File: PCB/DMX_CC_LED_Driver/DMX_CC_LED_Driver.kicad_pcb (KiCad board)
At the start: 2 copper layers, 100 x 45 mm, 46 parts, among them J1 Programming_Header, J2 PWR_OUT, J3 PWR_IN, J4 PWR_IN, J5 Conn_Left, J6 Conn_Right, SW1 SW_SPST, SW2 SW_DIP_x04, U2 MAX485E, U3 ATmega328P-AU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

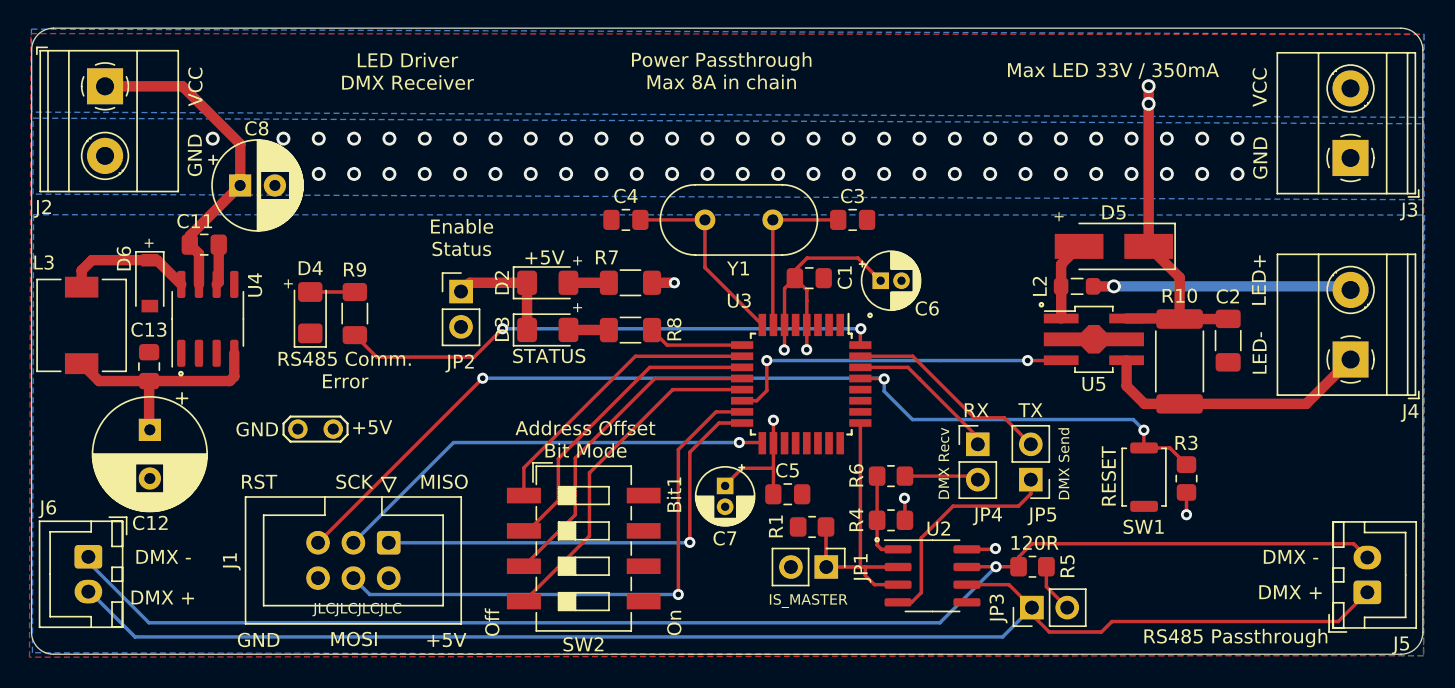
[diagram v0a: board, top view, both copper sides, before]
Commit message: Started work on PWM LED Driver and fixed small spelling mistakes
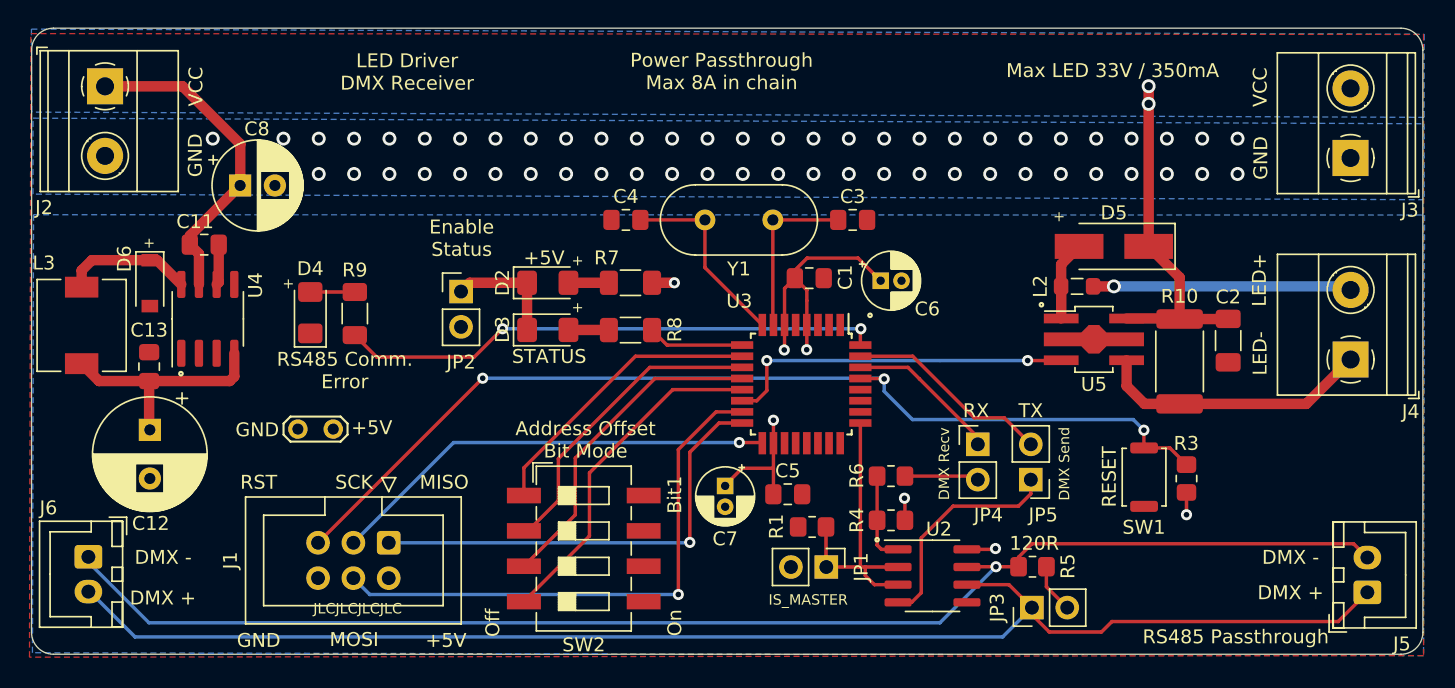
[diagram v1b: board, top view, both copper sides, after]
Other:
- net class Default removed
